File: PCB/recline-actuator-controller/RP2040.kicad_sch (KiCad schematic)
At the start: 27 parts, among them J1 DX07S016JA1R1500, J2 Conn_01x03, SW1 TL3330AF260QG, SW2 TL3330AF260QG, U1 TEMPLATE, U2 RP2040, X1 ABM8G-12.000MHZ-18-D2Y-T

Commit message: Recline Actuator Control
Recline controller board schematic and Recline actuator board schematics. Actuator control board schematic 90% complete.
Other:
- note added: "MCU - RP2040"

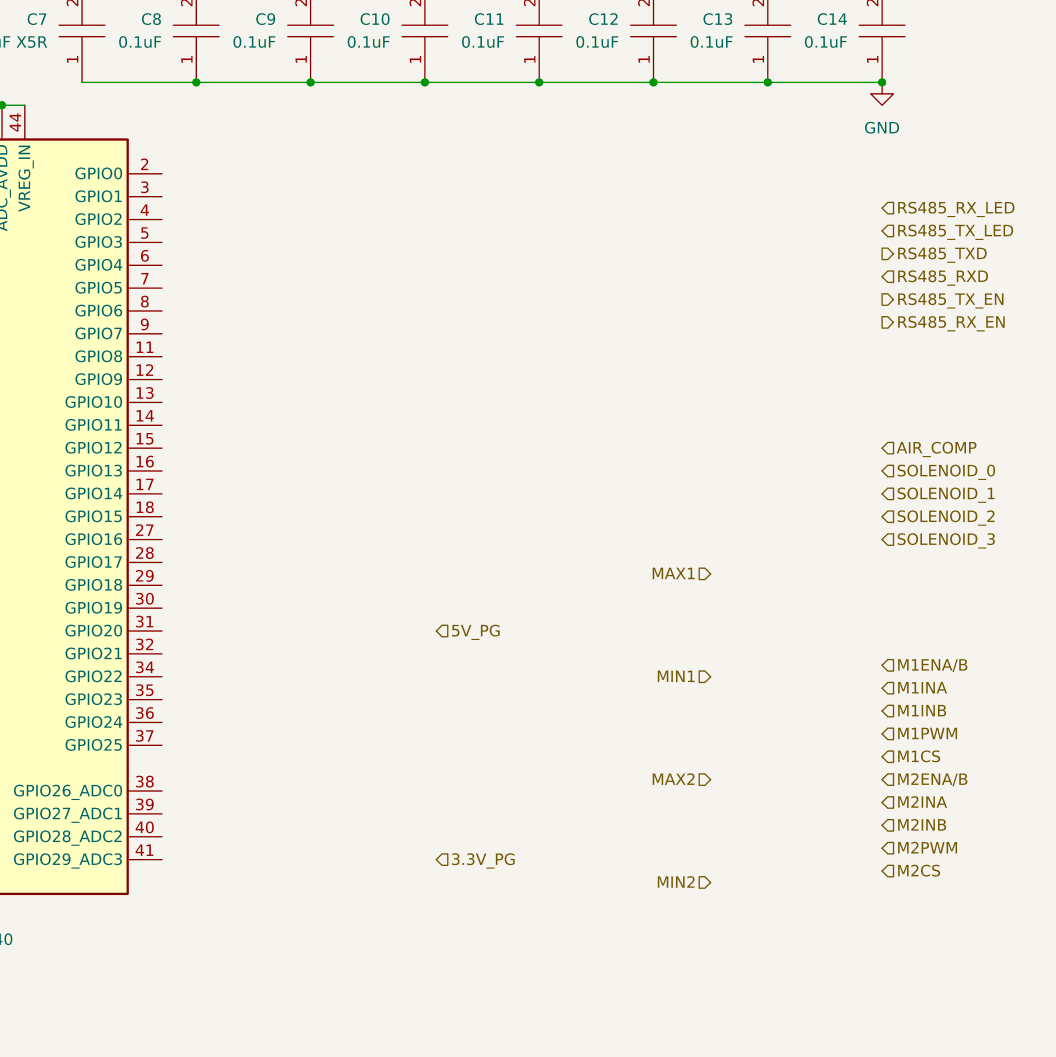
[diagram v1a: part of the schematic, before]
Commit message: Actuator Control Schematic
Schematic for Actuator control board completed! Once reviewed PCB layout will start.
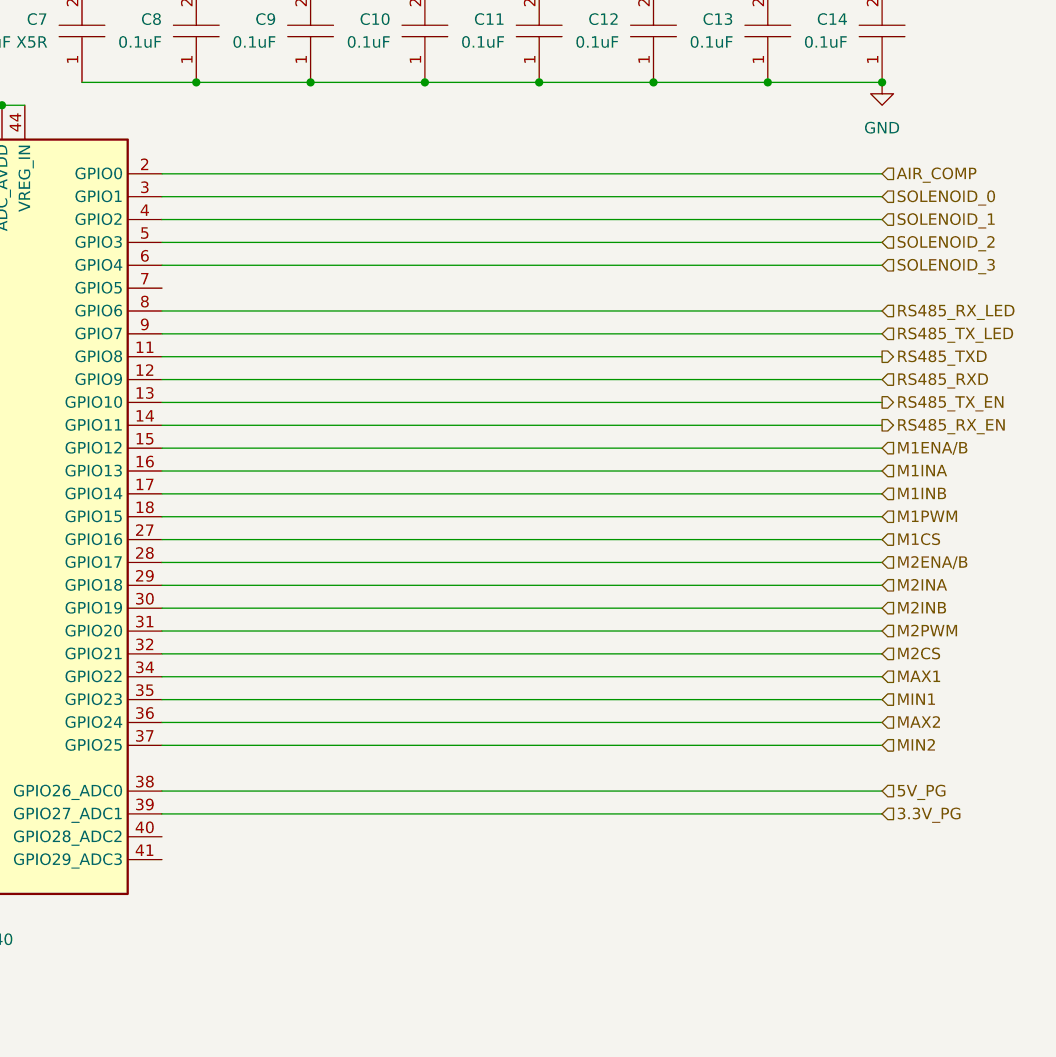
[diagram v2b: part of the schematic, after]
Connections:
- net 3.3V_PG: now also U2.39 (GPIO27_ADC1)
- net 5V_PG: now also U2.38 (GPIO26_ADC0)
- net AIR_COMP: now also U2.2 (GPIO0)
- net M1CS: now also U2.27 (GPIO16)
- net M1ENA/B: now also U2.15 (GPIO12)
- net M1INA: now also U2.16 (GPIO13)
- net M1INB: now also U2.17 (GPIO14)
- net M1PWM: now also U2.18 (GPIO15)
- net M2CS: now also U2.32 (GPIO21)
- net M2ENA/B: now also U2.28 (GPIO17)
- net M2INA: now also U2.29 (GPIO18)
- net M2INB: now also U2.30 (GPIO19)
- net M2PWM: now also U2.31 (GPIO20)
- net MAX1: now also U2.34 (GPIO22)
- net MAX2: now also U2.36 (GPIO24)
- net MIN1: now also U2.35 (GPIO23)
- net MIN2: now also U2.37 (GPIO25)
- net RS485_RXD: now also U2.12 (GPIO9)
- net RS485_RX_EN: now also U2.14 (GPIO11)
- net RS485_RX_LED: now also U2.8 (GPIO6)
- net RS485_TXD: now also U2.11 (GPIO8)
- net RS485_TX_EN: now also U2.13 (GPIO10)
- net RS485_TX_LED: now also U2.9 (GPIO7)
- net SOLENOID_0: now also U2.3 (GPIO1)
- net SOLENOID_1: now also U2.4 (GPIO2)
- net SOLENOID_2: now also U2.5 (GPIO3)
- net SOLENOID_3: now also U2.6 (GPIO4)

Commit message: Recline Actuator Control PCB
Recline Actuator Control PCB created. Still need to figure out board shape and connector placement.
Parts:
- C2, C4: footprint growbox-KiCAD-Capacitors:C0402 -> AVR-KiCAD-Lib-Capacitors:C0402
- J2: footprint (none) -> Connector_PinHeader_2.54mm:PinHeader_1x03_P2.54mm_Vertical
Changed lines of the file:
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@@
 			)
 		)
-		(property "Footprint" ""
+		(property "Footprint" "Connector_PinHeader_2.54mm:PinHeader_1x03_P2.54mm_Vertical"
 			(at 64.77 139.7 0)
 			(effects
@@
 			)
 		)
-		(property "Footprint" "growbox-KiCAD-Capacitors:C0402"
+		(property "Footprint" "AVR-KiCAD-Lib-Capacitors:C0402"
 			(at 99.06 129.54 0)
 			(effects
@@
 			)
 		)
-		(property "Footprint" "growbox-KiCAD-Capacitors:C0402"
+		(property "Footprint" "AVR-KiCAD-Lib-Capacitors:C0402"
 			(at 114.3 129.54 0)
 			(effects

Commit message: First Pass of PCB
First pass of PCB complete, needs review.
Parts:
- removed R4, R5: RC1206FR-075K1L, AVR-KiCAD-Lib-Resistors:R1206, symbol AVR-KiCAD-Lib-Resistors:RC1206FR-075K1L
- added R4, R5: RC0402FR-075K1L, AVR-KiCAD-Lib-Resistors:R0402, symbol AVR-KiCAD-Lib-Resistors:RC0402FR-075K1L
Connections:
- net 3.3V_PG: now also U2.40 (GPIO28_ADC2); no longer U2.39 (GPIO27_ADC1)
- net 5V_PG: now also U2.39 (GPIO27_ADC1); no longer U2.38 (GPIO26_ADC0)
- net AIR_COMP: now also U2.34 (GPIO22); no longer U2.2 (GPIO0)
- net GND: now also R4.2, R5.2
- net M1CS: now also U2.8 (GPIO6); no longer U2.27 (GPIO16)
- net M1ENA/B: now also U2.11 (GPIO8); no longer U2.15 (GPIO12)
- net M1INA: now also U2.12 (GPIO9); no longer U2.16 (GPIO13)
- net M1INB: now also U2.7 (GPIO5); no longer U2.17 (GPIO14)
- net M1PWM: now also U2.9 (GPIO7); no longer U2.18 (GPIO15)
- net M2CS: now also U2.4 (GPIO2); no longer U2.32 (GPIO21)
- net M2ENA/B: now also U2.3 (GPIO1); no longer U2.28 (GPIO17)
- net M2INA: now also U2.6 (GPIO4); no longer U2.29 (GPIO18)
- net M2INB: now also U2.2 (GPIO0); no longer U2.30 (GPIO19)
- net M2PWM: now also U2.5 (GPIO3); no longer U2.31 (GPIO20)
- net MAX1: now also U2.14 (GPIO11); no longer U2.34 (GPIO22)
- net MAX2: now also U2.16 (GPIO13); no longer U2.36 (GPIO24)
- net MIN1: now also U2.15 (GPIO12); no longer U2.35 (GPIO23)
- net MIN2: now also U2.17 (GPIO14); no longer U2.37 (GPIO25)
- net RS485_RXD: now also U2.28 (GPIO17); no longer U2.12 (GPIO9)
- net RS485_RX_EN: now also U2.30 (GPIO19); no longer U2.14 (GPIO11)
- net RS485_RX_LED: now also U2.31 (GPIO20); no longer U2.8 (GPIO6)
- net RS485_TXD: now also U2.27 (GPIO16); no longer U2.11 (GPIO8)
- net RS485_TX_EN: now also U2.29 (GPIO18); no longer U2.13 (GPIO10)
- net RS485_TX_LED: now also U2.32 (GPIO21); no longer U2.9 (GPIO7)
- net SOLENOID_0: now also U2.38 (GPIO26_ADC0); no longer U2.3 (GPIO1)
- net SOLENOID_1: now also U2.37 (GPIO25); no longer U2.4 (GPIO2)
- net SOLENOID_2: now also U2.36 (GPIO24); no longer U2.5 (GPIO3)
- net SOLENOID_3: now also U2.35 (GPIO23); no longer U2.6 (GPIO4)
- net at J1.3 (CC1): now also R5.1
- net at J1.9 (CC2): now also R4.1
